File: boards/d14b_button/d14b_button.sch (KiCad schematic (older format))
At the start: 35 parts, among them SW1 SW_PUSH, SW2 SW_PUSH, U2 nRF24L01+-Module

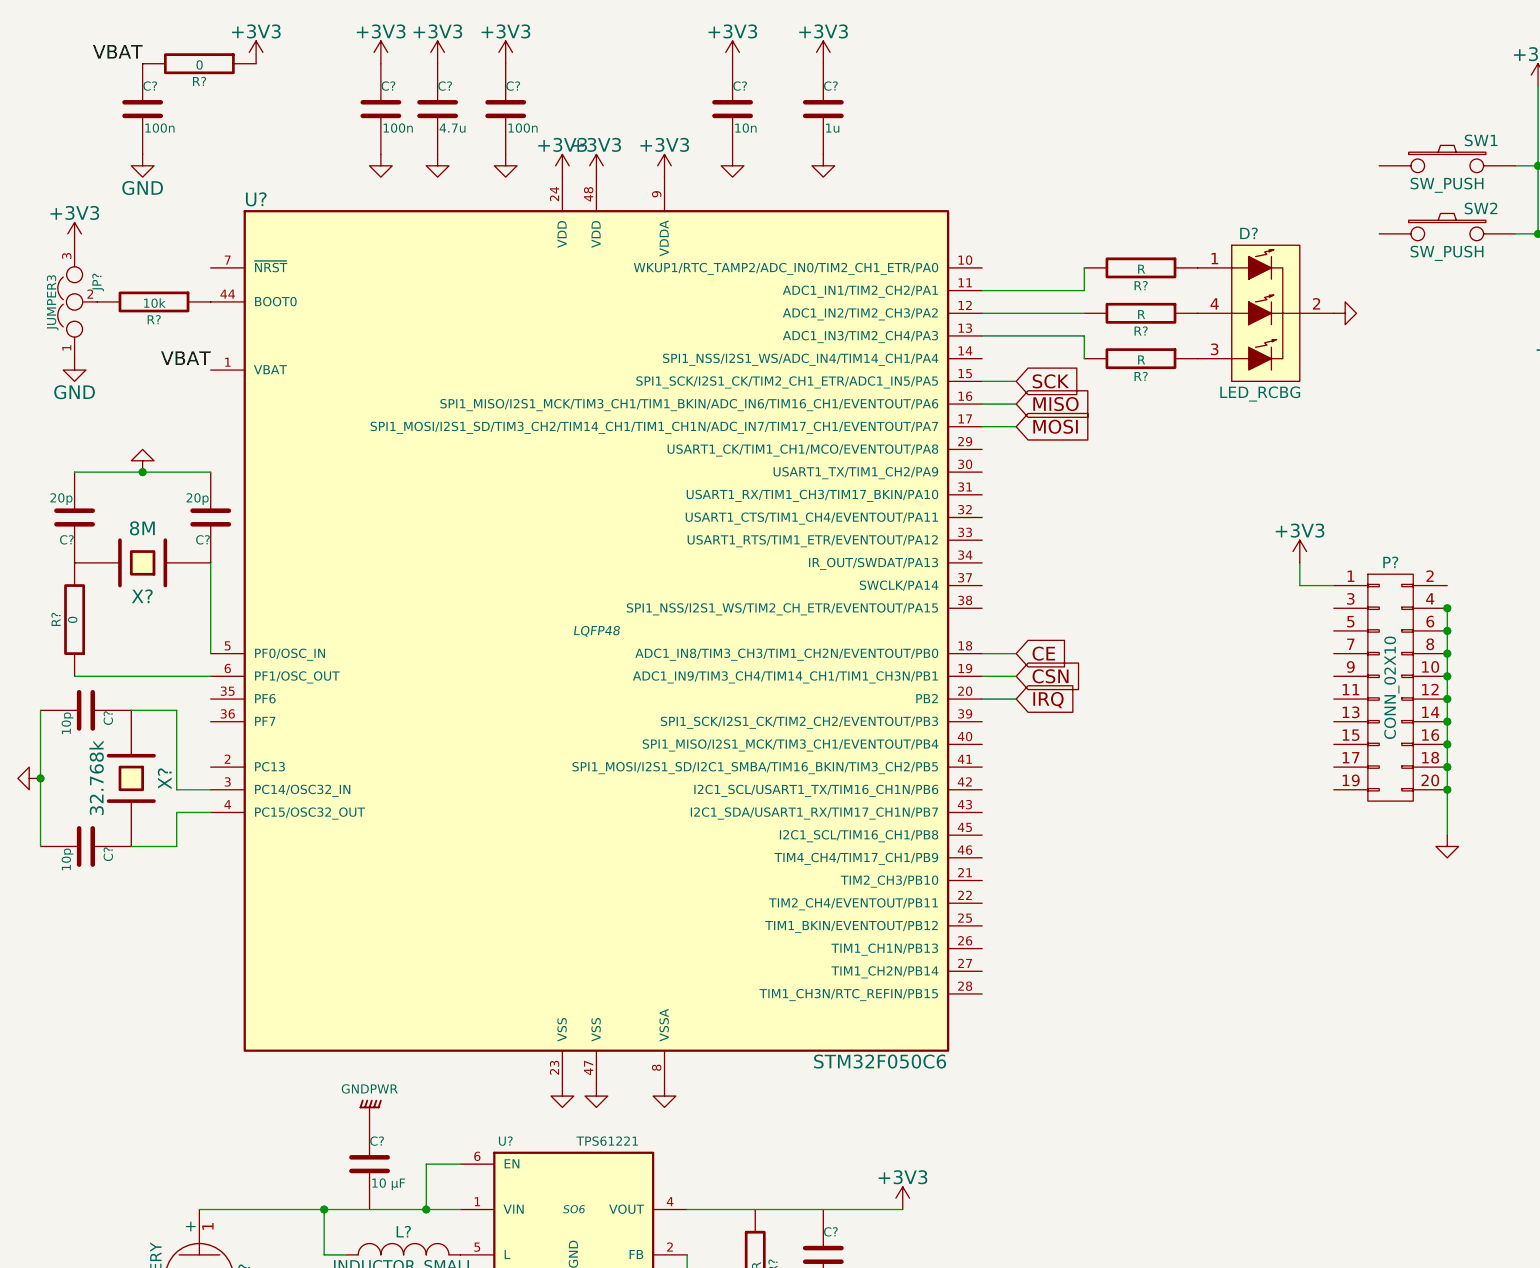
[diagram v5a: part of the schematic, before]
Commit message: Schaltplan um Mikrocontroller etwas aufgehübscht
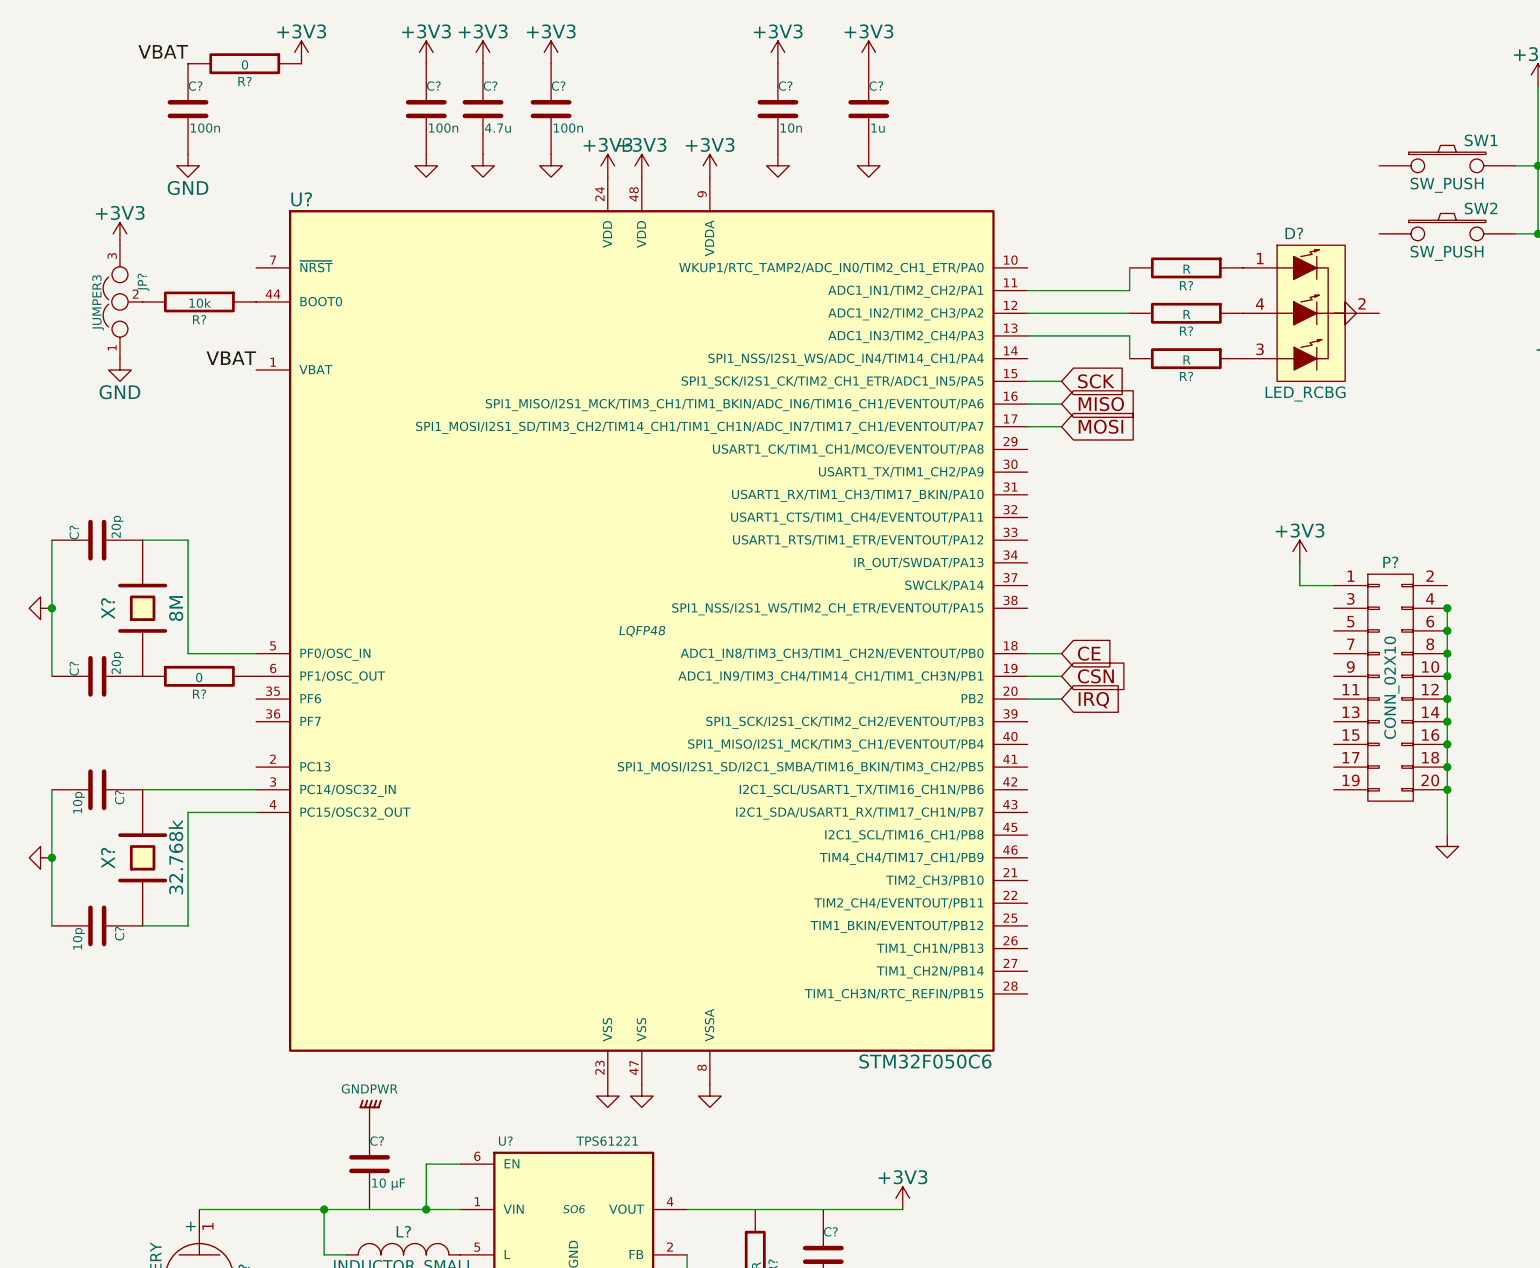
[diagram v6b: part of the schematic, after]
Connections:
- net GND: now also C?.1, C?.1; no longer C?.2, C?.2, D?.2 (COMMON_CATHODE)
- net at C?.1, U?.3 (PC14/OSC32_IN): now also X?.2; no longer X?.1
- net at C?.1, U?.4 (PC15/OSC32_OUT): now also X?.1; no longer X?.2
- net at R?.1: now also C?.2, X?.1; no longer U?.6 (PF1/OSC_OUT)
- new net: C?.2, U?.5 (PF0/OSC_IN), X?.2
- new net: R?.2, U?.6 (PF1/OSC_OUT)
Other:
- moved on the sheet: C?, D?, JP?, R?, U?, X?

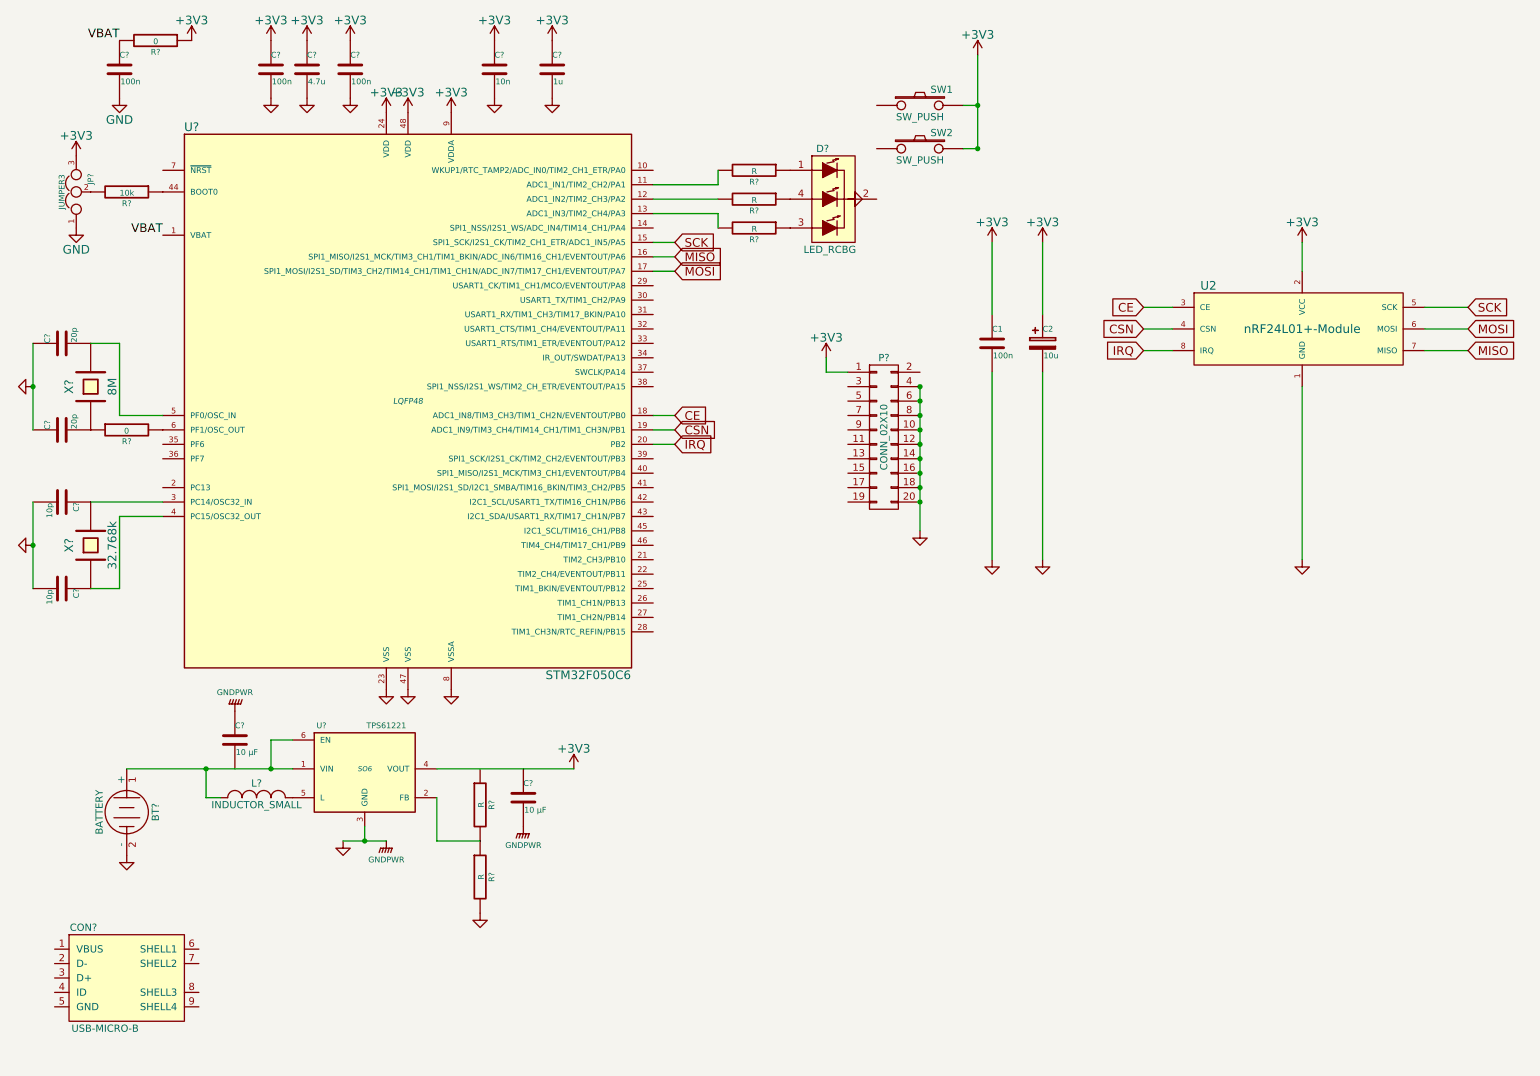
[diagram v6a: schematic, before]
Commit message: Schaltplan aufgeräumt
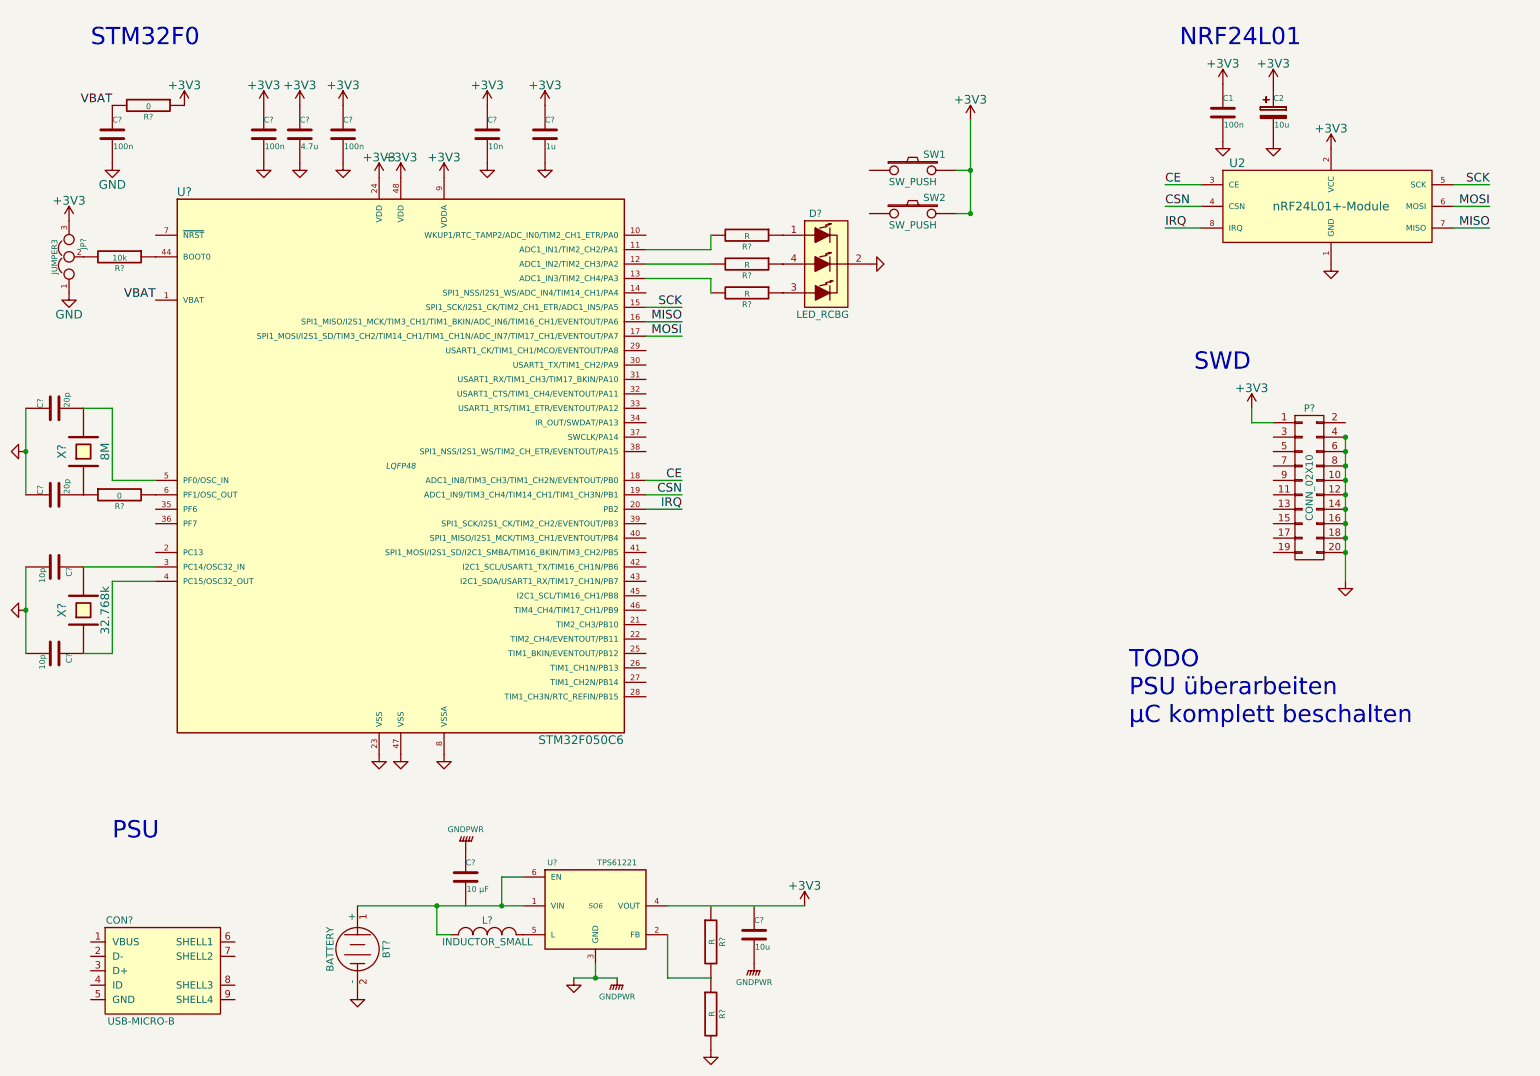
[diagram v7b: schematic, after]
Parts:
- C?: value 10 μF -> 10u
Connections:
- net GND: now also D?.2 (COMMON_CATHODE)
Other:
- note added: "NRF24L01"
- note added: "PSU"
- note added: "STM32F0"
- note added: "SWD"
- note added: "TODO\nPSU überarbeiten\nµC komplett beschalten"
- moved on the sheet: BT?, C1, C2, C?, CON?, D?, JP?, L?, P?, R?, SW1, SW2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

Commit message: UART angeschlossen
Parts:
- added P?: CONN_01X03, symbol CONN_01X03
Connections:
- net GND: now also P?.3 (P3)
- net UARTTX: now reaches U?.30 (USART1_TX/TIM1_CH2/PA9)
- net UARTTX: now also P?.2 (P2)
- net UARTRX: now reaches U?.31 (USART1_RX/TIM1_CH3/TIM17_BKIN/PA10)
- net UARTRX: now also P?.1 (P1)
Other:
- note added: "UART\n"
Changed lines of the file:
@@
 Text Label 8500 2000 0    60   ~ 0
 IRQ
-Text Label 5150 2550 2    60   ~ 0
+Text Label 5250 2550 2    60   ~ 0
 SCK
-Text Label 5150 2650 2    60   ~ 0
+Text Label 5250 2650 2    60   ~ 0
 MISO
-Text Label 5150 2750 2    60   ~ 0
+Text Label 5250 2750 2    60   ~ 0
 MOSI
-Text Label 5150 3750 2    60   ~ 0
+Text Label 5250 3750 2    60   ~ 0
 CE
-Text Label 5150 3850 2    60   ~ 0
+Text Label 5250 3850 2    60   ~ 0
 CSN
-Text Label 5150 3950 2    60   ~ 0
+Text Label 5250 3950 2    60   ~ 0
 IRQ
 Wire Wire Line
-	4900 2550 5150 2550
+	4900 2550 5250 2550
 Wire Wire Line
-	4900 2650 5150 2650
+	4900 2650 5250 2650
 Wire Wire Line
-	4900 2750 5150 2750
+	4900 2750 5250 2750
 Wire Wire Line
-	5150 3750 4900 3750
+	4900 3750 5250 3750
 Wire Wire Line
-	4900 3850 5150 3850
+	4900 3850 5250 3850
 Wire Wire Line
-	4900 3950 5150 3950
+	4900 3950 5250 3950
 Wire Wire Line
 	8500 1700 8750 1700
@@
 Text Notes 1200 6250 0    120  ~ 0
 PSU
-Text Notes 8250 5450 0    120  ~ 0
+Text Notes 5750 5800 0    120  ~ 0
 TODO\nPSU überarbeiten\nµC komplett beschalten
+Text Notes 8750 5000 0    120  ~ 0
+UART\n
+$Comp
+L CONN_01X03 P?
+U 1 1 54B08A26
+P 9500 5400
+F 0 "P?" H 9500 5600 50  0000 C CNN
+F 1 "CONN_01X03" V 9600 5400 50  0000 C CNN
+F 2 "" H 9500 5400 60  0000 C CNN
+F 3 "" H 9500 5400 60  0000 C CNN
+	1    9500 5400
+	1    0    0    -1
+$EndComp
+Wire Wire Line
+	8900 5300 9300 5300
+Wire Wire Line
+	8900 5400 9300 5400
+Text Label 8900 5300 0    60   ~ 0
+UARTRX
+Text Label 8900 5400 0    60   ~ 0
+UARTTX
+$Comp
+L GND #PWR?
+U 1 1 54B08EA3
+P 9300 5500
+F 0 "#PWR?" H 9300 5250 60  0001 C CNN
+F 1 "GND" H 9300 5350 60  0000 C CNN
+F 2 "" H 9300 5500 60  0000 C CNN
+F 3 "" H 9300 5500 60  0000 C CNN
+	1    9300 5500
+	1    0    0    -1
+$EndComp
+Text Label 5250 3050 2    60   ~ 0
+UARTRX
+Text Label 5250 2950 2    60   ~ 0
+UARTTX
+Wire Wire Line
+	5250 2950 4900 2950
+Wire Wire Line
+	4900 3050 5250 3050
 $EndSCHEMATC
